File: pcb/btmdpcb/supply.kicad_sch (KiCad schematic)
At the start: 15 parts, among them J1 USB_C_Receptacle_PowerOnly_6P, Q1 AO3401A, U4 TP4057

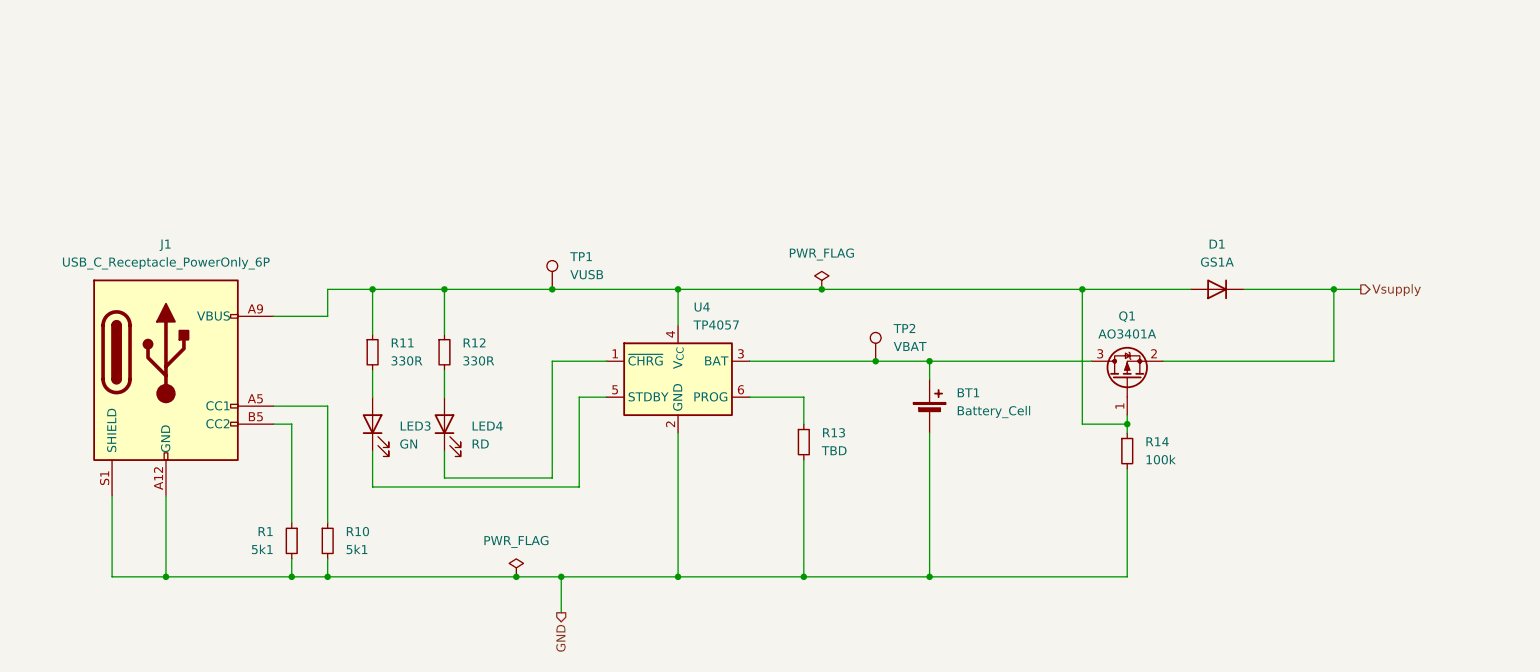
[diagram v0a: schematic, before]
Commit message: Clean up schematic, implement all logic functionality
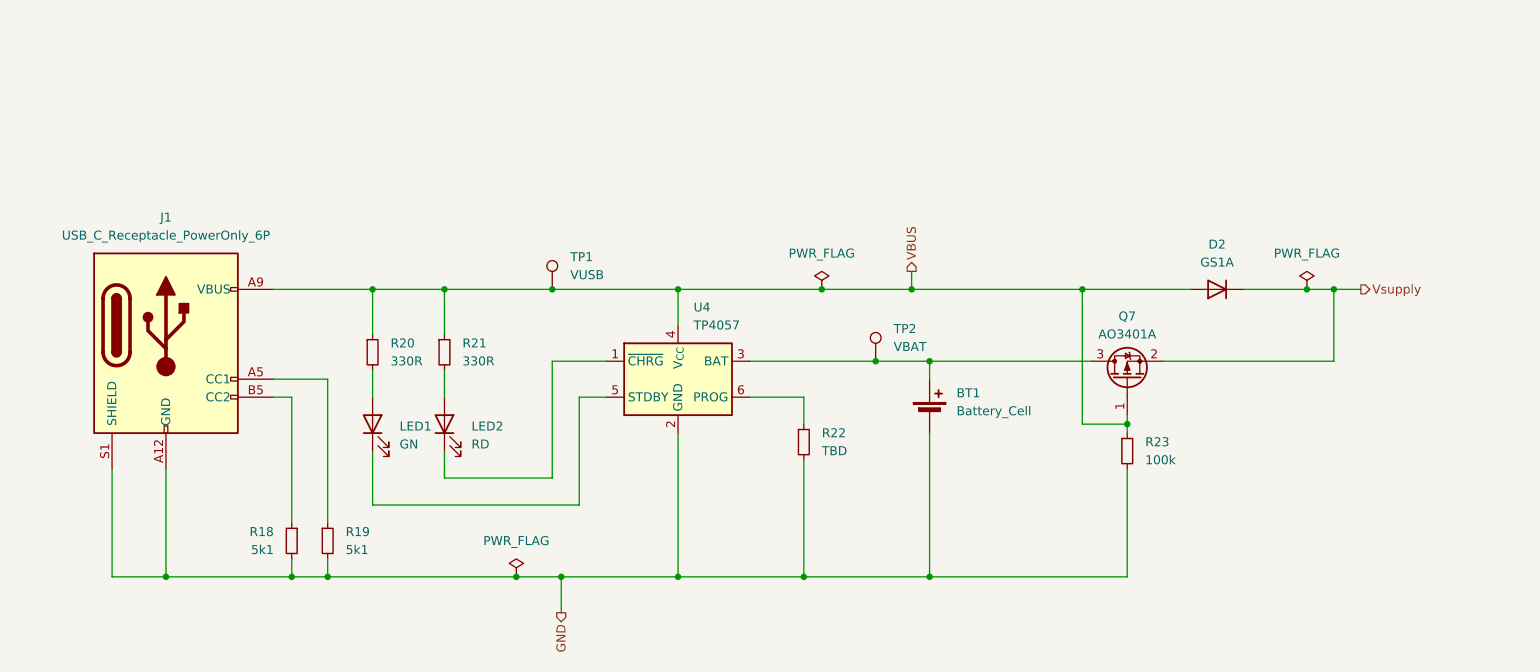
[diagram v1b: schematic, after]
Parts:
- renumbered D1 to D2, LED3 to LED1, LED4 to LED2, Q1 to Q7, R1 to R18, R10 to R19, R11 to R20, R12 to R21, R13 to R22, R14 to R23
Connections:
- net VBUS: now reaches D2.2 (A), J1.A9 (VBUS), J1.B9 (VBUS), Q7.1 (G), R20.1, R21.1, R23.1, TP1.1, U4.4 (V_{CC})
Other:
- moved on the sheet: J1
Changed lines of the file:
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@@
+	)
+	(junction
+		(at 233.68 63.5)
+		(diameter 0)
+		(color 0 0 0 0)
 	)
 	(junction
@@
 	)
 	(junction
+		(at 177.8 63.5)
+		(diameter 0)
+		(color 0 0 0 0)
+	)
+	(junction
 		(at 208.28 82.55)
 		(diameter 0)
@@
 	(wire
 		(pts
-			(xy 90.17 82.55) (xy 90.17 96.52)
+			(xy 90.17 78.74) (xy 90.17 96.52)
 		)
 		(stroke
@@
 	(wire
 		(pts
+			(xy 177.8 63.5) (xy 177.8 60.96)
+		)
+		(stroke
+			(width 0)
+			(type default)
+		)
+	)
+	(wire
+		(pts
 			(xy 180.34 83.82) (xy 180.34 104.14)
 		)
@@
 	(wire
 		(pts
-			(xy 224.79 63.5) (xy 237.49 63.5)
+			(xy 224.79 63.5) (xy 233.68 63.5)
 		)
 		(stroke
@@
 	(wire
 		(pts
-			(xy 87.63 80.01) (xy 95.25 80.01)
-		)
-		(stroke
-			(width 0)
-			(type default)
-		)
-	)
-	(wire
-		(pts
-			(xy 95.25 63.5) (xy 101.6 63.5)
+			(xy 87.63 76.2) (xy 95.25 76.2)
 		)
 		(stroke
@@
 	(wire
 		(pts
-			(xy 95.25 80.01) (xy 95.25 96.52)
+			(xy 95.25 76.2) (xy 95.25 96.52)
 		)
 		(stroke
@@
 	(wire
 		(pts
-			(xy 165.1 63.5) (xy 201.93 63.5)
+			(xy 165.1 63.5) (xy 177.8 63.5)
 		)
 		(stroke
@@
 	(wire
 		(pts
-			(xy 87.63 67.31) (xy 95.25 67.31)
+			(xy 87.63 63.5) (xy 101.6 63.5)
 		)
 		(stroke
@@
 	(wire
 		(pts
+			(xy 233.68 63.5) (xy 237.49 63.5)
+		)
+		(stroke
+			(width 0)
+			(type default)
+		)
+	)
+	(wire
+		(pts
 			(xy 101.6 74.93) (xy 101.6 78.74)
 		)
@@
 	(wire
 		(pts
-			(xy 101.6 91.44) (xy 130.81 91.44)
+			(xy 101.6 93.98) (xy 130.81 93.98)
 		)
 		(stroke
@@
 	(wire
 		(pts
-			(xy 101.6 86.36) (xy 101.6 91.44)
+			(xy 101.6 86.36) (xy 101.6 93.98)
 		)
 		(stroke
@@
 	(wire
 		(pts
+			(xy 177.8 63.5) (xy 201.93 63.5)
+		)
+		(stroke
+			(width 0)
+			(type default)
+		)
+	)
+	(wire
+		(pts
 			(xy 237.49 63.5) (xy 237.49 73.66)
 		)
@@
 	(wire
 		(pts
-			(xy 87.63 82.55) (xy 90.17 82.55)
+			(xy 87.63 78.74) (xy 90.17 78.74)
 		)
 		(stroke
@@
 	(wire
 		(pts
-			(xy 95.25 67.31) (xy 95.25 63.5)
-		)
-		(stroke
-			(width 0)
-			(type default)
-		)
-	)
-	(wire
-		(pts
 			(xy 111.76 74.93) (xy 111.76 78.74)
 		)
@@
 	(wire
 		(pts
-			(xy 72.39 104.14) (xy 72.39 92.71)
-		)
-		(stroke
-			(width 0)
-			(type default)
-		)
-	)
-	(wire
-		(pts
-			(xy 130.81 91.44) (xy 130.81 78.74)
+			(xy 72.39 104.14) (xy 72.39 88.9)
+		)
+		(stroke
+			(width 0)
+			(type default)
+		)
+	)
+	(wire
+		(pts
+			(xy 130.81 93.98) (xy 130.81 78.74)
 		)
 		(stroke
@@
 	(wire
 		(pts
-			(xy 64.77 104.14) (xy 64.77 92.71)
+			(xy 64.77 104.14) (xy 64.77 88.9)
 		)
 		(stroke
@@
 			(width 0)
 			(type default)
+		)
+	)
+	(hierarchical_label "VBUS"
+		(shape output)
+		(at 177.8 60.96 90)
+		(fields_autoplaced yes)
+		(effects
+			(font
+				(size 1.27 1.27)
+			)
+			(justify left)
 		)
 	)
@@
 		(dnp no)
 		(fields_autoplaced yes)
-		(property "Reference" "#FLG06"
+		(property "Reference" "#FLG05"
 			(at 165.1 61.595 0)
 			(effects
@@
 			(project ""
 				(path "/6e43e92f-e106-411c-86ee-217d084aee5b/30ff757b-83ca-4184-84db-39f939669bab"
-					(reference "#FLG06")
+					(reference "#FLG05")
 					(unit 1)
 				)
@@
 		(dnp no)
 		(fields_autoplaced yes)
-		(property "Reference" "Q1"
+		(property "Reference" "Q7"
 			(at 208.28 67.31 90)
 			(effects
@@
 			(project "btmdpcb"
 				(path "/6e43e92f-e106-411c-86ee-217d084aee5b/30ff757b-83ca-4184-84db-39f939669bab"
-					(reference "Q1")
+					(reference "Q7")
 					(unit 1)
 				)
@@
 		(dnp no)
 		(fields_autoplaced yes)
-		(property "Reference" "R11"
+		(property "Reference" "R20"
 			(at 104.14 71.1199 0)
 			(effects
@@
 			(project "btmdpcb"
 				(path "/6e43e92f-e106-411c-86ee-217d084aee5b/30ff757b-83ca-4184-84db-39f939669bab"
-					(reference "R11")
+					(reference "R20")
 					(unit 1)
 				)
@@
 		(dnp no)
 		(fields_autoplaced yes)
-		(property "Reference" "LED4"
+		(property "Reference" "LED2"
 			(at 115.57 82.8674 90)
 			(effects
@@
 			(project "btmdpcb"
 				(path "/6e43e92f-e106-411c-86ee-217d084aee5b/30ff757b-83ca-4184-84db-39f939669bab"
-					(reference "LED4")
+					(reference "LED2")
 					(unit 1)
 				)
@@
 		(dnp no)
 		(fields_autoplaced yes)
-		(property "Reference" "#FLG05"
+		(property "Reference" "#FLG04"
 			(at 121.92 102.235 0)
 			(effects
@@
 			(project ""
 				(path "/6e43e92f-e106-411c-86ee-217d084aee5b/30ff757b-83ca-4184-84db-39f939669bab"
-					(reference "#FLG05")
+					(reference "#FLG04")
 					(unit 1)
 				)
@@
 		(dnp no)
 		(fields_autoplaced yes)
-		(property "Reference" "R12"
+		(property "Reference" "R21"
 			(at 114.3 71.1199 0)
 			(effects
@@
 			(project "btmdpcb"
 				(path "/6e43e92f-e106-411c-86ee-217d084aee5b/30ff757b-83ca-4184-84db-39f939669bab"
-					(reference "R12")
+					(reference "R21")
 					(unit 1)
 				)
@@
 		(on_board yes)
 		(dnp no)
-		(property "Reference" "R13"
+		(property "Reference" "R22"
 			(at 165.1 83.8199 0)
 			(effects
@@
 			(project "btmdpcb"
 				(path "/6e43e92f-e106-411c-86ee-217d084aee5b/30ff757b-83ca-4184-84db-39f939669bab"
-					(reference "R13")
+					(reference "R22")
 					(unit 1)
 				)
@@
 		(dnp no)
 		(fields_autoplaced yes)
-		(property "Reference" "R1"
+		(property "Reference" "R18"
 			(at 87.63 97.7899 0)
 			(effects
@@
 			(project "btmdpcb"
 				(path "/6e43e92f-e106-411c-86ee-217d084aee5b/30ff757b-83ca-4184-84db-39f939669bab"
-					(reference "R1")
+					(reference "R18")
 					(unit 1)
 				)
@@
 		(dnp no)
 		(fields_autoplaced yes)
-		(property "Reference" "LED3"
+		(property "Reference" "LED1"
 			(at 105.41 82.8674 90)
 			(effects
@@
 			(project "btmdpcb"
 				(path "/6e43e92f-e106-411c-86ee-217d084aee5b/30ff757b-83ca-4184-84db-39f939669bab"
-					(reference "LED3")
+					(reference "LED1")
 					(unit 1)
 				)
@@
 		(dnp no)
 		(fields_autoplaced yes)
-		(property "Reference" "D1"
+		(property "Reference" "D2"
 			(at 220.98 57.15 0)
 			(effects
@@
 			(project "btmdpcb"
 				(path "/6e43e92f-e106-411c-86ee-217d084aee5b/30ff757b-83ca-4184-84db-39f939669bab"
-					(reference "D1")
+					(reference "D2")
 					(unit 1)
 				)
@@
 	(symbol
 		(lib_id "Connector:USB_C_Receptacle_PowerOnly_6P")
-		(at 72.39 74.93 0)
+		(at 72.39 71.12 0)
 		(unit 1)
 		(exclude_from_sim no)
@@
 		(fields_autoplaced yes)
 		(property "Reference" "J1"
-			(at 72.39 57.15 0)
+			(at 72.39 53.34 0)
 			(effects
 				(font
@@
 		)
 		(property "Value" "USB_C_Receptacle_PowerOnly_6P"
-			(at 72.39 59.69 0)
+			(at 72.39 55.88 0)
 			(effects
 				(font
@@
 		)
 		(property "Footprint" ""
-			(at 76.2 72.39 0)
+			(at 76.2 68.58 0)
 			(effects
 				(font
@@
 		)
 		(property "Datasheet" "https://www.usb.org/sites/default/files/documents/usb_type-c.zip"
-			(at 72.39 74.93 0)
+			(at 72.39 71.12 0)
 			(effects
 				(font
@@
 		)
 		(property "Description" "USB Power-Only 6P Type-C Receptacle connector"
-			(at 72.39 74.93 0)
+			(at 72.39 71.12 0)
 			(effects
 				(font
@@
 				(path "/6e43e92f-e106-411c-86ee-217d084aee5b/30ff757b-83ca-4184-84db-39f939669bab"
 					(reference "J1")
+					(unit 1)
+				)
+			)
+		)
+	)
+	(symbol
+		(lib_id "power:PWR_FLAG")
+		(at 233.68 63.5 0)
+		(unit 1)
+		(exclude_from_sim no)
+		(in_bom yes)
+		(on_board yes)
+		(dnp no)
+		(fields_autoplaced yes)
+		(property "Reference" "#FLG06"
+			(at 233.68 61.595 0)
+			(effects
+				(font
+					(size 1.27 1.27)
+				)
+				(hide yes)
+			)
+		)
+		(property "Value" "PWR_FLAG"
+			(at 233.68 58.42 0)
+			(effects
+				(font
+					(size 1.27 1.27)
+				)
+			)
+		)
+		(property "Footprint" ""
+			(at 233.68 63.5 0)
+			(effects
+				(font
+					(size 1.27 1.27)
+				)
+				(hide yes)
+			)
+		)
+		(property "Datasheet" "~"
+			(at 233.68 63.5 0)
+			(effects
+				(font
+					(size 1.27 1.27)
+				)
+				(hide yes)
+			)
+		)
+		(property "Description" "Special symbol for telling ERC where power comes from"
+			(at 233.68 63.5 0)
+			(effects
+				(font
+					(size 1.27 1.27)
+				)
+				(hide yes)
+			)
+		)
+		(pin "1"
+		)
+		(instances
+			(project "btmdpcb"
+				(path "/6e43e92f-e106-411c-86ee-217d084aee5b/30ff757b-83ca-4184-84db-39f939669bab"
+					(reference "#FLG06")
 					(unit 1)
 				)
@@
 		(dnp no)
 		(fields_autoplaced yes)
-		(property "Reference" "R14"
+		(property "Reference" "R23"
 			(at 210.82 85.0899 0)
 			(effects
@@
 			(project "btmdpcb"
 				(path "/6e43e92f-e106-411c-86ee-217d084aee5b/30ff757b-83ca-4184-84db-39f939669bab"
-					(reference "R14")
+					(reference "R23")
 					(unit 1)
 				)
@@
 		(dnp no)
 		(fields_autoplaced yes)
-		(property "Reference" "R10"
+		(property "Reference" "R19"
 			(at 97.79 97.7899 0)
 			(effects
@@
 			(project "btmdpcb"
 				(path "/6e43e92f-e106-411c-86ee-217d084aee5b/30ff757b-83ca-4184-84db-39f939669bab"
-					(reference "R10")
+					(reference "R19")
 					(unit 1)
 				)

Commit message: Remove redundant regulators, simplify schematic
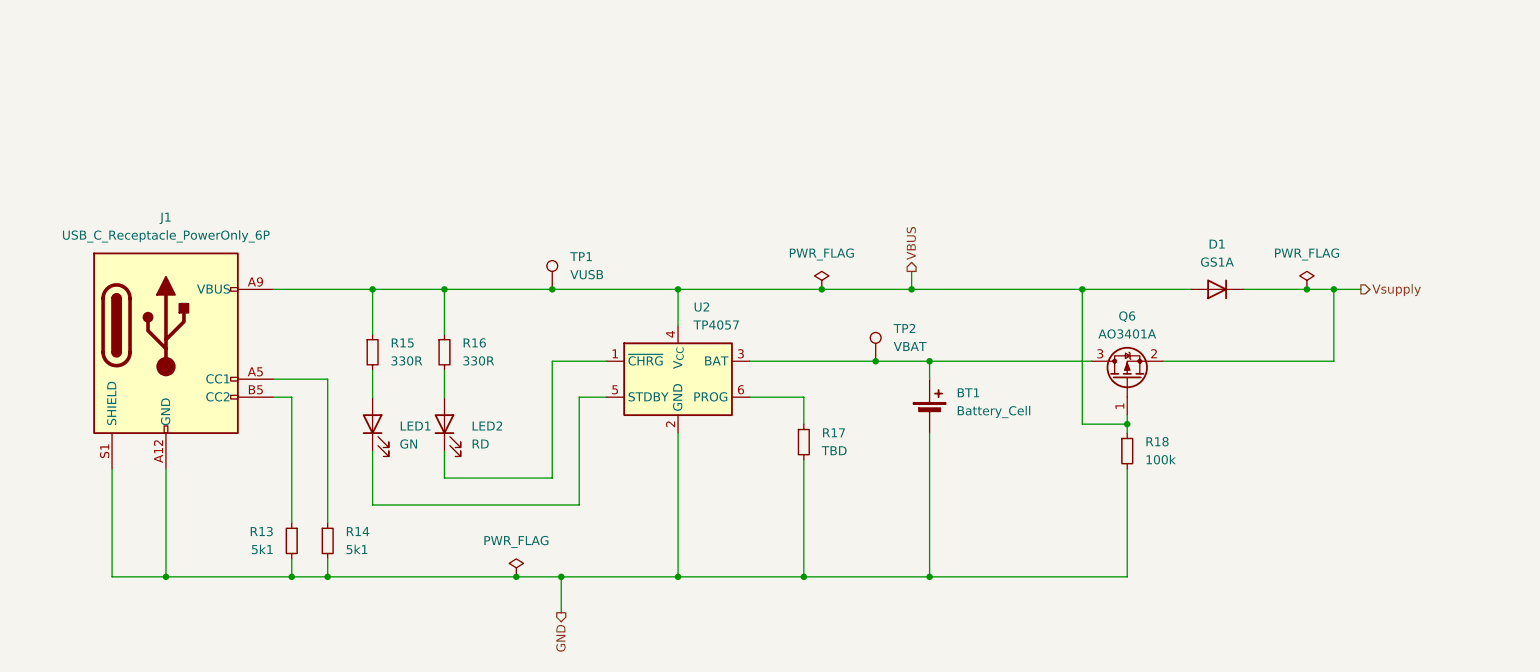
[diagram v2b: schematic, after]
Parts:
- renumbered D2 to D1, Q7 to Q6, R18 to R13, R19 to R14, R20 to R15, R21 to R16, R22 to R17, R23 to R18, U4 to U2
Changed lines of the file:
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@@
 		(dnp no)
 		(fields_autoplaced yes)
-		(property "Reference" "#FLG05"
+		(property "Reference" "#FLG03"
 			(at 165.1 61.595 0)
 			(effects
@@
 			(project ""
 				(path "/6e43e92f-e106-411c-86ee-217d084aee5b/30ff757b-83ca-4184-84db-39f939669bab"
-					(reference "#FLG05")
+					(reference "#FLG03")
 					(unit 1)
 				)
@@
 		(dnp no)
 		(fields_autoplaced yes)
-		(property "Reference" "Q7"
+		(property "Reference" "Q6"
 			(at 208.28 67.31 90)
 			(effects
@@
 			(project "btmdpcb"
 				(path "/6e43e92f-e106-411c-86ee-217d084aee5b/30ff757b-83ca-4184-84db-39f939669bab"
-					(reference "Q7")
+					(reference "Q6")
 					(unit 1)
 				)
@@
 		(dnp no)
 		(fields_autoplaced yes)
-		(property "Reference" "R20"
+		(property "Reference" "R15"
 			(at 104.14 71.1199 0)
 			(effects
@@
 			(project "btmdpcb"
 				(path "/6e43e92f-e106-411c-86ee-217d084aee5b/30ff757b-83ca-4184-84db-39f939669bab"
-					(reference "R20")
+					(reference "R15")
 					(unit 1)
 				)
@@
 		(dnp no)
 		(fields_autoplaced yes)
-		(property "Reference" "#FLG04"
+		(property "Reference" "#FLG02"
 			(at 121.92 102.235 0)
 			(effects
@@
 			(project ""
 				(path "/6e43e92f-e106-411c-86ee-217d084aee5b/30ff757b-83ca-4184-84db-39f939669bab"
-					(reference "#FLG04")
+					(reference "#FLG02")
 					(unit 1)
 				)
@@
 		(dnp no)
 		(fields_autoplaced yes)
-		(property "Reference" "R21"
+		(property "Reference" "R16"
 			(at 114.3 71.1199 0)
 			(effects
@@
 			(project "btmdpcb"
 				(path "/6e43e92f-e106-411c-86ee-217d084aee5b/30ff757b-83ca-4184-84db-39f939669bab"
-					(reference "R21")
+					(reference "R16")
 					(unit 1)
 				)
@@
 		(on_board yes)
 		(dnp no)
-		(property "Reference" "R22"
+		(property "Reference" "R17"
 			(at 165.1 83.8199 0)
 			(effects
@@
 			(project "btmdpcb"
 				(path "/6e43e92f-e106-411c-86ee-217d084aee5b/30ff757b-83ca-4184-84db-39f939669bab"
-					(reference "R22")
+					(reference "R17")
 					(unit 1)
 				)
@@
 		(dnp no)
 		(fields_autoplaced yes)
-		(property "Reference" "R18"
+		(property "Reference" "R13"
 			(at 87.63 97.7899 0)
 			(effects
@@
 			(project "btmdpcb"
 				(path "/6e43e92f-e106-411c-86ee-217d084aee5b/30ff757b-83ca-4184-84db-39f939669bab"
-					(reference "R18")
+					(reference "R13")
 					(unit 1)
 				)
@@
 		(dnp no)
 		(fields_autoplaced yes)
-		(property "Reference" "U4"
+		(property "Reference" "U2"
 			(at 146.9741 66.04 0)
 			(effects
@@
 			(project "btmdpcb"
 				(path "/6e43e92f-e106-411c-86ee-217d084aee5b/30ff757b-83ca-4184-84db-39f939669bab"
-					(reference "U4")
+					(reference "U2")
 					(unit 1)
 				)
@@
 		(dnp no)
 		(fields_autoplaced yes)
-		(property "Reference" "D2"
+		(property "Reference" "D1"
 			(at 220.98 57.15 0)
 			(effects
@@
 			(project "btmdpcb"
 				(path "/6e43e92f-e106-411c-86ee-217d084aee5b/30ff757b-83ca-4184-84db-39f939669bab"
-					(reference "D2")
+					(reference "D1")
 					(unit 1)
 				)
@@
 		(dnp no)
 		(fields_autoplaced yes)
-		(property "Reference" "#FLG06"
+		(property "Reference" "#FLG04"
 			(at 233.68 61.595 0)
 			(effects
@@
 			(project "btmdpcb"
 				(path "/6e43e92f-e106-411c-86ee-217d084aee5b/30ff757b-83ca-4184-84db-39f939669bab"
-					(reference "#FLG06")
+					(reference "#FLG04")
 					(unit 1)
 				)
@@
 		(dnp no)
 		(fields_autoplaced yes)
-		(property "Reference" "R23"
+		(property "Reference" "R18"
 			(at 210.82 85.0899 0)
 			(effects
@@
 			(project "btmdpcb"
 				(path "/6e43e92f-e106-411c-86ee-217d084aee5b/30ff757b-83ca-4184-84db-39f939669bab"
-					(reference "R23")
+					(reference "R18")
 					(unit 1)
 				)
@@
 		(dnp no)
 		(fields_autoplaced yes)
-		(property "Reference" "R19"
+		(property "Reference" "R14"
 			(at 97.79 97.7899 0)
 			(effects
@@
 			(project "btmdpcb"
 				(path "/6e43e92f-e106-411c-86ee-217d084aee5b/30ff757b-83ca-4184-84db-39f939669bab"
-					(reference "R19")
-					(unit 1)
-				)
+					(reference "R14")
+					(unit 1)
+				)

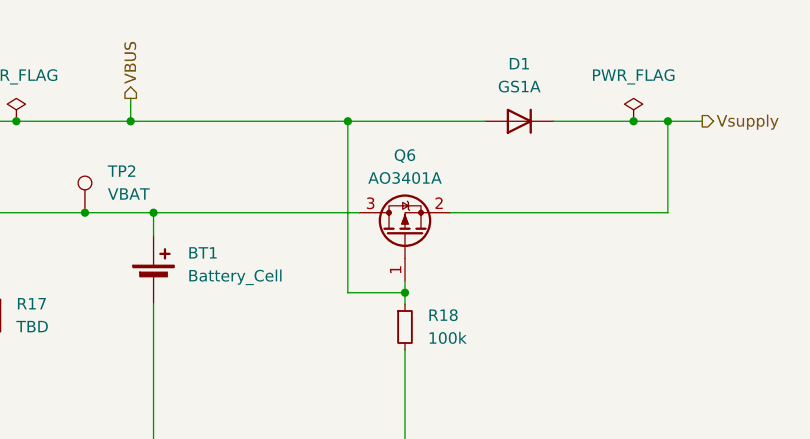
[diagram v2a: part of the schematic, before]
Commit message: Add BT auto-powerup (RC circuit + comparator)
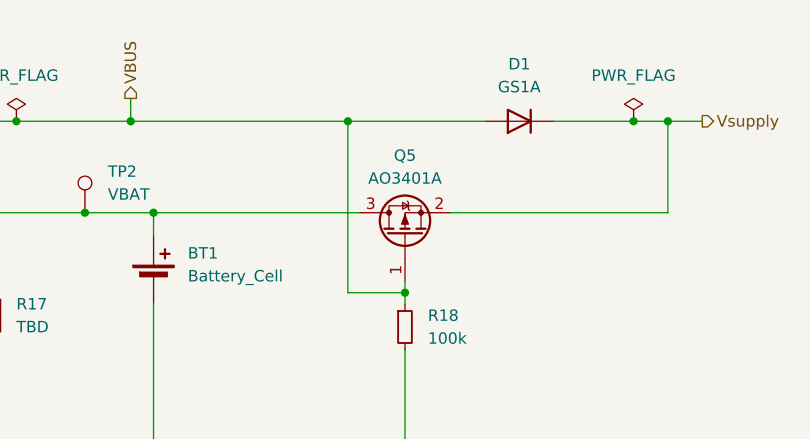
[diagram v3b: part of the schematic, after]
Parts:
- renumbered Q6 to Q5
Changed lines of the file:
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@@
 		(dnp no)
 		(fields_autoplaced yes)
-		(property "Reference" "Q6"
+		(property "Reference" "Q5"
 			(at 208.28 67.31 90)
 			(effects
@@
 			(project "btmdpcb"
 				(path "/6e43e92f-e106-411c-86ee-217d084aee5b/30ff757b-83ca-4184-84db-39f939669bab"
-					(reference "Q6")
+					(reference "Q5")
 					(unit 1)
 				)
